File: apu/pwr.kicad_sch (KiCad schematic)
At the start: 198 parts, among them U1 X818336-001

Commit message: Cleanup & Debug I/O
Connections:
- net V_CPUPLL renamed +1.8V

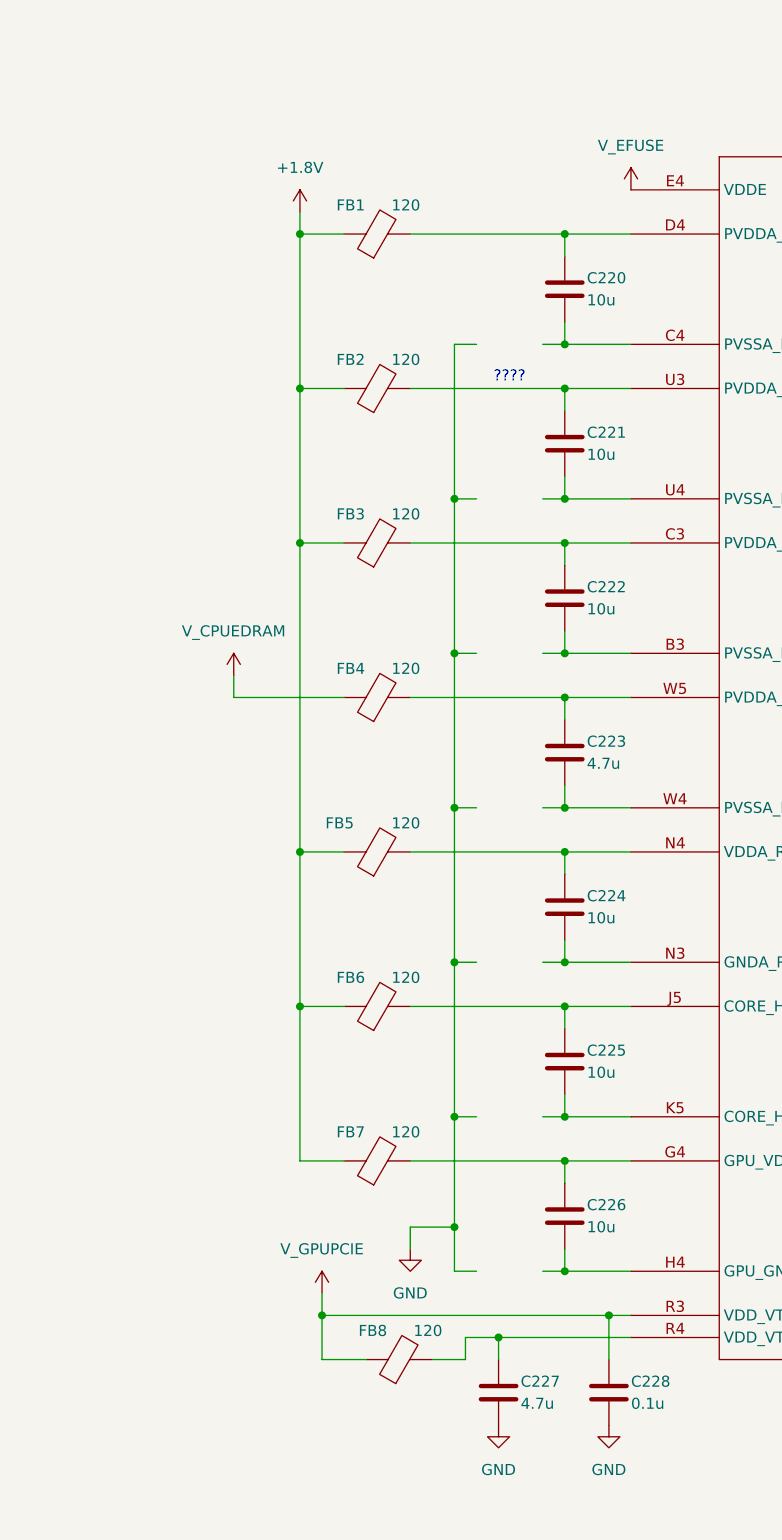
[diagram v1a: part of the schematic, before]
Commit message: Nand Flash, Sata Connectors and removing (hopefully) unnecessary things
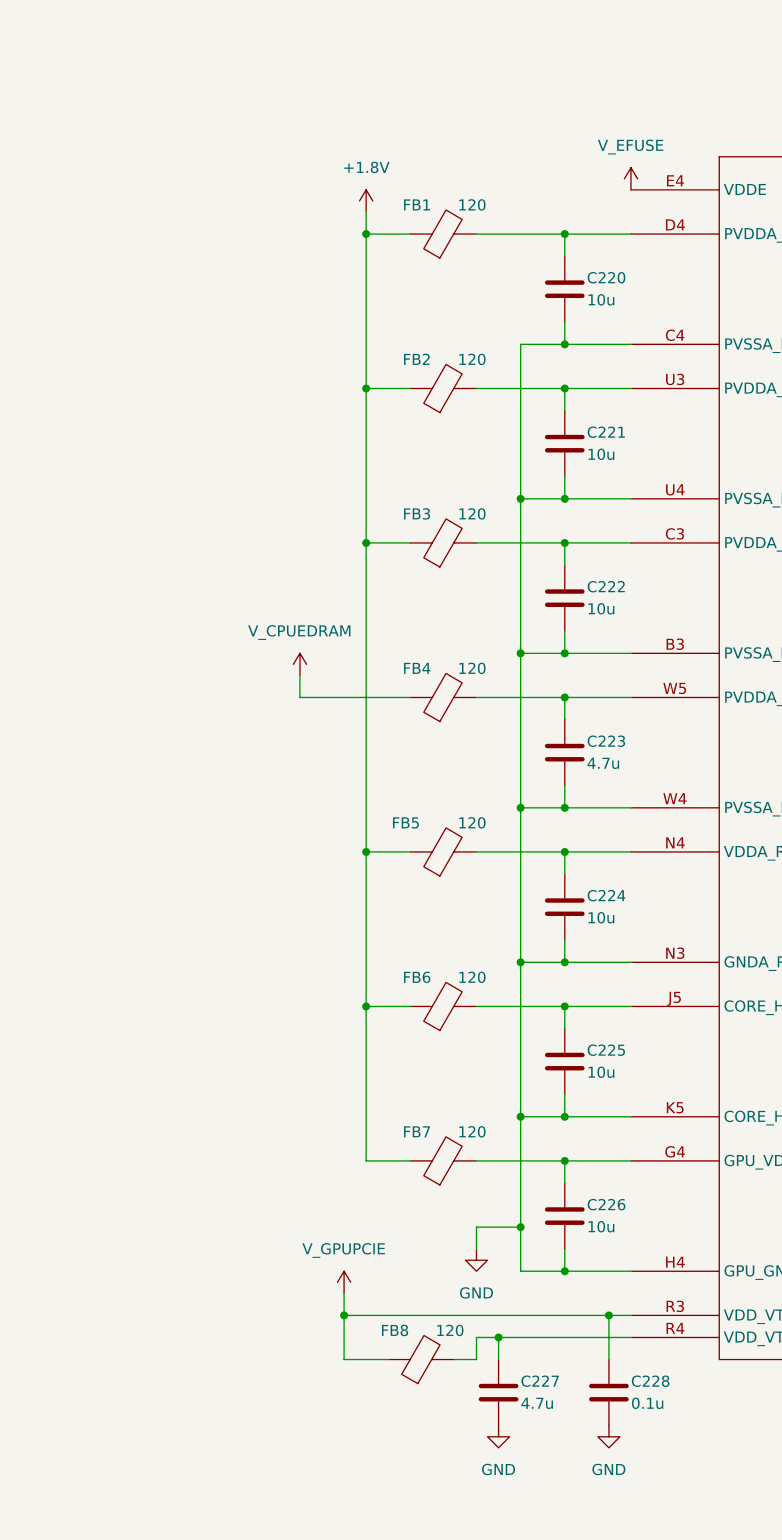
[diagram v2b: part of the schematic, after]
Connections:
- net GND: now also C220.2, C221.2, C222.2, C223.2, C224.2, C225.2, C226.2, U1.B3 (PVSSA_HS), U1.C4 (PVSSA_MEM), U1.H4 (GPU_GNDA_PLL), U1.K5 (CORE_HF_GNDA_PLL), U1.N3 (GNDA_RNG), U1.U4 (PVSSA_PEX), U1.W4 (PVSSA_ED)
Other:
- note removed: "????"
- moved on the sheet: FB1, FB2, FB3, FB4, FB5, FB6, FB7, FB8

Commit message: Multipurpose and standby power rails, Reannotated schematic
Added V_1P2, V_1P8, V_5P0DUAL, V_EFUSE, V_GPUPCIE, V_3P3STBY and V_1P2STBY
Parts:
- renumbered C66 to C100, C85 to C101, C104 to C102, C122 to C103, C140 to C104, C157 to C105, C174 to C106, C191 to C107, C208 to C108, C227 to C109, C48 to C110, C67 to C111, C86 to C112, C105 to C113, C123 to C114, C141 to C115, C158 to C116, C175 to C117, C192 to C118, C209 to C119, C220 to C120, C221 to C121, C222 to C122, C223 to C123, C224 to C124, C225 to C125, C226 to C126, C228 to C127, C49 to C128, C68 to C129, C87 to C130, C106 to C131, C124 to C132, C142 to C133, C159 to C134, C176 to C135, C193 to C136, C210 to C137, C50 to C138, C69 to C139, C88 to C140, C107 to C141, C125 to C142, C160 to C144, C177 to C145, C194 to C146, C211 to C147, C51 to C148, C70 to C149, C89 to C150, C108 to C151, C126 to C152, C144 to C153, C161 to C154, C178 to C155, C195 to C156, C212 to C157, C52 to C158, C71 to C159, C90 to C160, C109 to C161, C127 to C162, C145 to C163, C162 to C164, C179 to C165, C196 to C166, C213 to C167, C53 to C168, C72 to C169, C91 to C170, C110 to C171, C128 to C172, C146 to C173, C163 to C174, C180 to C175, C197 to C176, C214 to C177, C54 to C178, C73 to C179, C92 to C180, C111 to C181, C129 to C182, C147 to C183, C164 to C184, C181 to C185, C198 to C186, C215 to C187, C55 to C188, C74 to C189, C93 to C190, C112 to C191, C130 to C192, C148 to C193, C165 to C194, C182 to C195, C199 to C196, C216 to C197, C56 to C198, C75 to C199, C94 to C200, C113 to C201, C131 to C202, C149 to C203, C166 to C204, C183 to C205, C200 to C206, C57 to C207, C76 to C208, C95 to C209, C114 to C210, C132 to C211, C150 to C212, C167 to C213, C184 to C214, C201 to C215, C217 to C216, C58 to C217, C77 to C218, C96 to C219, C115 to C220, C133 to C221, C151 to C222, C168 to C223, C185 to C224, C202 to C225, C218 to C226, C40 to C38, C59 to C39, C78 to C40, C97 to C41, C116 to C42, C134 to C43, C41 to C44, C60 to C45, C79 to C46, C98 to C47, C42 to C48, C61 to C49, C80 to C50, C99 to C51, C117 to C52, C135 to C53, C152 to C54, C169 to C55, C186 to C56, C203 to C57, C43 to C58, C62 to C59, C81 to C60, C100 to C61, C118 to C62, C136 to C63, C153 to C64, C170 to C65, C187 to C66, C204 to C67, C44 to C68, C63 to C69, C82 to C70, C101 to C71, C119 to C72, C137 to C73, C154 to C74, C171 to C75, C188 to C76, C205 to C77, C45 to C78, C64 to C79, C83 to C80, C102 to C81, C120 to C82, C138 to C83, C155 to C84, C172 to C85, C189 to C86, C206 to C87, C219 to C88, C46 to C89, C65 to C90, C84 to C91, C103 to C92, C121 to C93, C139 to C94, C156 to C95, C173 to C96, C190 to C97, C207 to C98, C47 to C99, FB8 to FB1, FB1 to FB2, FB2 to FB3, FB3 to FB4, FB4 to FB5, FB5 to FB6, FB6 to FB7, FB7 to FB8
